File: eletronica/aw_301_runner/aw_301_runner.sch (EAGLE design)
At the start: 7 parts, among them IC1 ATTINY2313V

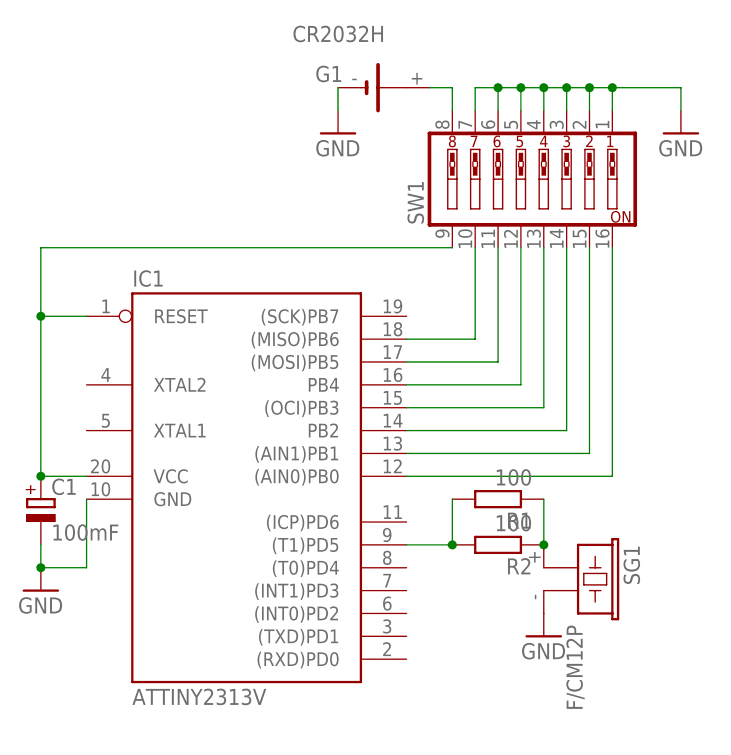
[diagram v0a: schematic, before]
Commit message: 
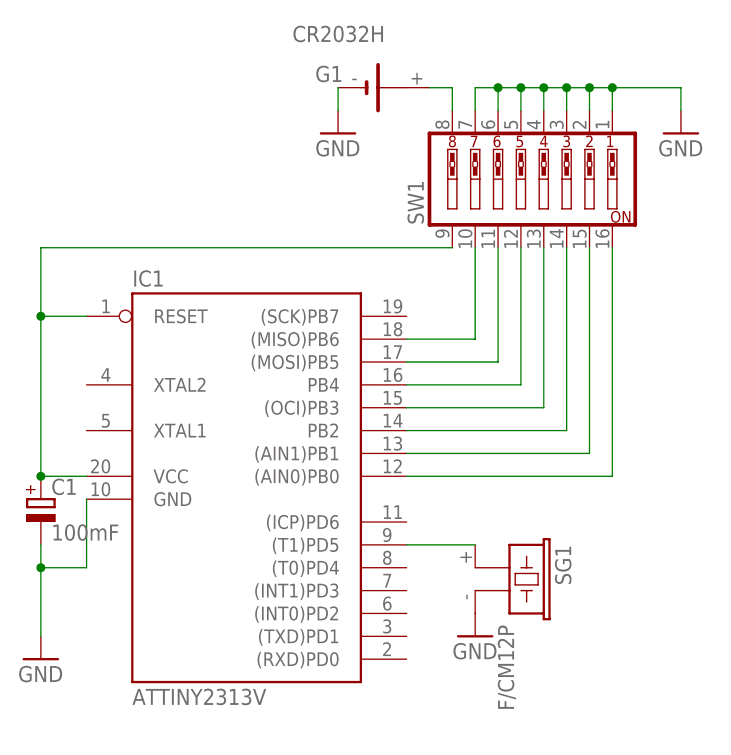
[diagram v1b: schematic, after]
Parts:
- removed R1, R2: 100, rcl:R-EU_0207/10
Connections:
- removed net N$2: IC1.(T1)PD5, R1.2, R2.2
- removed net N$3: R1.1, R2.1, SG1.1
- new net N$1: IC1.(T1)PD5, SG1.1
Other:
- moved on the sheet: SG1
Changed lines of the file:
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@@
 <part name="G1" library="battery" deviceset="CR2032H" device=""/>
 <part name="C1" library="resistor" deviceset="CPOL-EU" device="E2.5-6" value="100mF"/>
-<part name="R2" library="rcl" deviceset="R-EU_" device="0207/10" value="100"/>
 <part name="GND2" library="supply1" deviceset="GND" device=""/>
 <part name="GND3" library="supply1" deviceset="GND" device=""/>
@@
 <part name="GND1" library="supply1" deviceset="GND" device=""/>
 <part name="GND4" library="supply1" deviceset="GND" device=""/>
-<part name="R1" library="rcl" deviceset="R-EU_" device="0207/10" value="100"/>
 </parts>
 <sheets>
@@
 </instance>
 <instance part="C1" gate="G$1" x="71.12" y="30.48"/>
-<instance part="R2" gate="G$1" x="121.92" y="25.4" rot="R180"/>
 <instance part="GND2" gate="1" x="104.14" y="71.12"/>
-<instance part="GND3" gate="1" x="71.12" y="20.32"/>
-<instance part="SG1" gate="G$1" x="129.54" y="22.86" rot="R270"/>
-<instance part="GND1" gate="1" x="127" y="15.24"/>
+<instance part="GND3" gate="1" x="71.12" y="12.7"/>
+<instance part="SG1" gate="G$1" x="121.92" y="22.86" rot="R270"/>
+<instance part="GND1" gate="1" x="119.38" y="15.24"/>
 <instance part="GND4" gate="1" x="142.24" y="71.12"/>
-<instance part="R1" gate="G$1" x="121.92" y="30.48" rot="R180"/>
 </instances>
 <busses>
@@
 <pinref part="C1" gate="G$1" pin="-"/>
 <pinref part="GND3" gate="1" pin="GND"/>
+<wire x1="71.12" y1="15.24" x2="71.12" y2="22.86" width="0.1524" layer="91"/>
+<pinref part="IC1" gate="G$1" pin="GND"/>
 <wire x1="71.12" y1="22.86" x2="71.12" y2="25.4" width="0.1524" layer="91"/>
-<pinref part="IC1" gate="G$1" pin="GND"/>
 <wire x1="76.2" y1="30.48" x2="76.2" y2="22.86" width="0.1524" layer="91"/>
 <wire x1="76.2" y1="22.86" x2="71.12" y2="22.86" width="0.1524" layer="91"/>
@@
 <wire x1="142.24" y1="76.2" x2="142.24" y2="73.66" width="0.1524" layer="91"/>
 <junction x="134.62" y="76.2"/>
-</segment>
-</net>
-<net name="N$2" class="0">
-<segment>
-<pinref part="IC1" gate="G$1" pin="(T1)PD5"/>
-<pinref part="R2" gate="G$1" pin="2"/>
-<wire x1="116.84" y1="25.4" x2="111.76" y2="25.4" width="0.1524" layer="91"/>
-<pinref part="R1" gate="G$1" pin="2"/>
-<wire x1="116.84" y1="25.4" x2="116.84" y2="30.48" width="0.1524" layer="91"/>
-<junction x="116.84" y="25.4"/>
-</segment>
-</net>
-<net name="N$3" class="0">
-<segment>
-<pinref part="R2" gate="G$1" pin="1"/>
-<pinref part="SG1" gate="G$1" pin="1"/>
-<pinref part="R1" gate="G$1" pin="1"/>
-<wire x1="127" y1="30.48" x2="127" y2="25.4" width="0.1524" layer="91"/>
-<junction x="127" y="25.4"/>
 </segment>
 </net>
@@
 </segment>
 </net>
+<net name="N$1" class="0">
+<segment>
+<pinref part="IC1" gate="G$1" pin="(T1)PD5"/>
+<pinref part="SG1" gate="G$1" pin="1"/>
+<wire x1="111.76" y1="25.4" x2="119.38" y2="25.4" width="0.1524" layer="91"/>
+</segment>
+</net>

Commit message: 
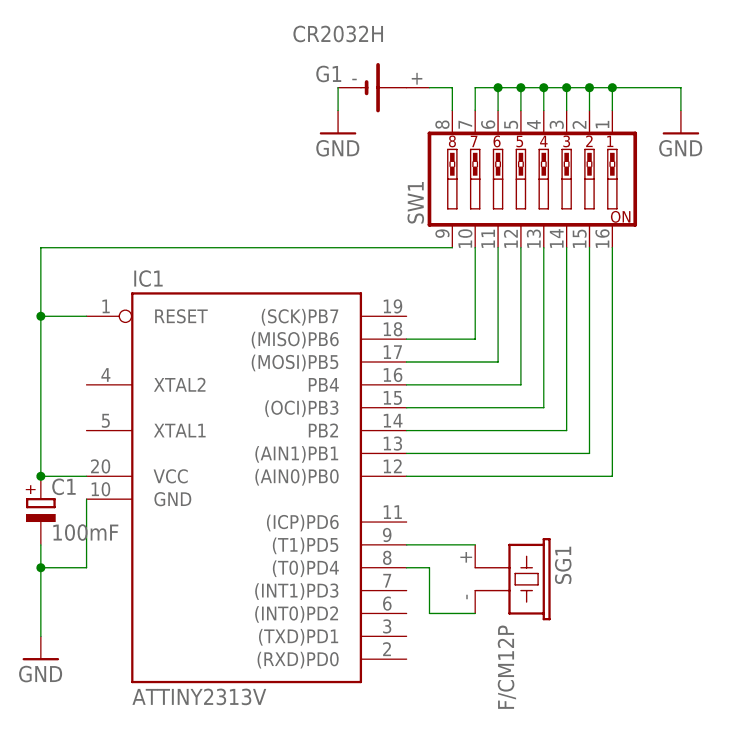
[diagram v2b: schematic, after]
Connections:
- new net N$2: IC1.(T0)PD4, SG1.2
- net GND: no longer SG1.2
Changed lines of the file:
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@@
 <part name="GND3" library="supply1" deviceset="GND" device=""/>
 <part name="SG1" library="buzzer" deviceset="F/CM12P" device=""/>
-<part name="GND1" library="supply1" deviceset="GND" device=""/>
 <part name="GND4" library="supply1" deviceset="GND" device=""/>
 </parts>
@@
 <instance part="GND3" gate="1" x="71.12" y="12.7"/>
 <instance part="SG1" gate="G$1" x="121.92" y="22.86" rot="R270"/>
-<instance part="GND1" gate="1" x="119.38" y="15.24"/>
 <instance part="GND4" gate="1" x="142.24" y="71.12"/>
 </instances>
@@
 <wire x1="76.2" y1="22.86" x2="71.12" y2="22.86" width="0.1524" layer="91"/>
 <junction x="71.12" y="22.86"/>
-</segment>
-<segment>
-<pinref part="SG1" gate="G$1" pin="2"/>
-<pinref part="GND1" gate="1" pin="GND"/>
 </segment>
 <segment>
@@
 </segment>
 </net>
+<net name="N$2" class="0">
+<segment>
+<pinref part="IC1" gate="G$1" pin="(T0)PD4"/>
+<wire x1="111.76" y1="22.86" x2="114.3" y2="22.86" width="0.1524" layer="91"/>
+<wire x1="114.3" y1="22.86" x2="114.3" y2="17.78" width="0.1524" layer="91"/>
+<pinref part="SG1" gate="G$1" pin="2"/>
+<wire x1="114.3" y1="17.78" x2="119.38" y2="17.78" width="0.1524" layer="91"/>
+</segment>
+</net>

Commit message: 
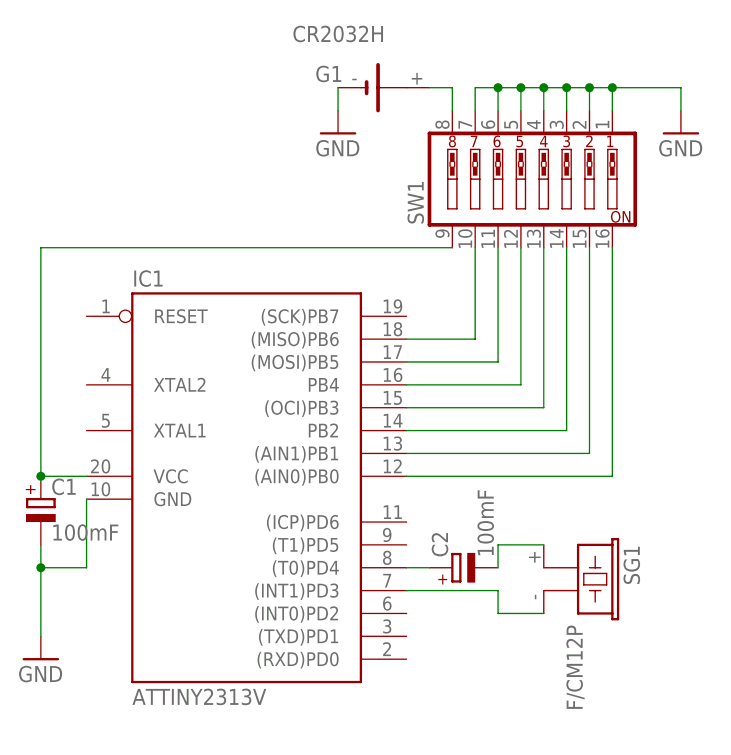
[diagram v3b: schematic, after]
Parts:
- added C2: 100mF, resistor:CPOL-EUE2.5-6
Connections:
- new net N$3: C2.-, SG1.1
- net N$1: now also IC1.(INT1)PD3, SG1.2; no longer IC1.(T1)PD5, SG1.1
- net N$2: now also C2.+; no longer SG1.2
- net N$5: no longer IC1.RESET
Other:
- moved on the sheet: SG1
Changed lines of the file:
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@@
 <part name="SG1" library="buzzer" deviceset="F/CM12P" device=""/>
 <part name="GND4" library="supply1" deviceset="GND" device=""/>
+<part name="C2" library="resistor" deviceset="CPOL-EU" device="E2.5-6" value="100mF"/>
 </parts>
 <sheets>
@@
 <instance part="GND2" gate="1" x="104.14" y="71.12"/>
 <instance part="GND3" gate="1" x="71.12" y="12.7"/>
-<instance part="SG1" gate="G$1" x="121.92" y="22.86" rot="R270"/>
+<instance part="SG1" gate="G$1" x="129.54" y="22.86" rot="R270"/>
 <instance part="GND4" gate="1" x="142.24" y="71.12"/>
+<instance part="C2" gate="G$1" x="116.84" y="22.86" rot="R90"/>
 </instances>
 <busses>
@@
 <wire x1="71.12" y1="33.02" x2="76.2" y2="33.02" width="0.1524" layer="91"/>
 <junction x="71.12" y="33.02"/>
-<wire x1="71.12" y1="58.42" x2="71.12" y2="50.8" width="0.1524" layer="91"/>
-<pinref part="IC1" gate="G$1" pin="RESET"/>
-<wire x1="71.12" y1="50.8" x2="71.12" y2="33.02" width="0.1524" layer="91"/>
-<wire x1="76.2" y1="50.8" x2="71.12" y2="50.8" width="0.1524" layer="91"/>
-<junction x="71.12" y="50.8"/>
+<wire x1="71.12" y1="58.42" x2="71.12" y2="33.02" width="0.1524" layer="91"/>
 </segment>
 </net>
@@
 </segment>
 </net>
-<net name="N$1" class="0">
-<segment>
-<pinref part="IC1" gate="G$1" pin="(T1)PD5"/>
-<pinref part="SG1" gate="G$1" pin="1"/>
-<wire x1="111.76" y1="25.4" x2="119.38" y2="25.4" width="0.1524" layer="91"/>
-</segment>
-</net>
 <net name="N$2" class="0">
 <segment>
 <pinref part="IC1" gate="G$1" pin="(T0)PD4"/>
 <wire x1="111.76" y1="22.86" x2="114.3" y2="22.86" width="0.1524" layer="91"/>
-<wire x1="114.3" y1="22.86" x2="114.3" y2="17.78" width="0.1524" layer="91"/>
-<pinref part="SG1" gate="G$1" pin="2"/>
-<wire x1="114.3" y1="17.78" x2="119.38" y2="17.78" width="0.1524" layer="91"/>
+<pinref part="C2" gate="G$1" pin="+"/>
 </segment>
 </net>
+<net name="N$1" class="0">
+<segment>
+<pinref part="IC1" gate="G$1" pin="(INT1)PD3"/>
+<wire x1="111.76" y1="20.32" x2="121.92" y2="20.32" width="0.1524" layer="91"/>
+<wire x1="121.92" y1="20.32" x2="121.92" y2="17.78" width="0.1524" layer="91"/>
+<pinref part="SG1" gate="G$1" pin="2"/>
+<wire x1="121.92" y1="17.78" x2="127" y2="17.78" width="0.1524" layer="91"/>
+</segment>
+</net>
+<net name="N$3" class="0">
+<segment>
+<pinref part="C2" gate="G$1" pin="-"/>
+<wire x1="121.92" y1="22.86" x2="121.92" y2="25.4" width="0.1524" layer="91"/>
+<pinref part="SG1" gate="G$1" pin="1"/>
+<wire x1="121.92" y1="25.4" x2="127" y2="25.4" width="0.1524" layer="91"/>
+</segment>
+</net>
